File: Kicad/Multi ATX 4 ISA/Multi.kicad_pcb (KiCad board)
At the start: 2 copper layers, 111.8 x 172.7 mm, 88 parts, among them J1 Bus_ISA_8bit, J10 Conn_02x08_Counter_Clockwise, J2 Mini-DIN-6, J3 SPK, J5 IRQ6 EN, J6 PWR ON, J7 Bus_ISA_8bit, J8 Bus_ISA_8bit, J9 Bus_ISA_8bit, SW1 RESET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

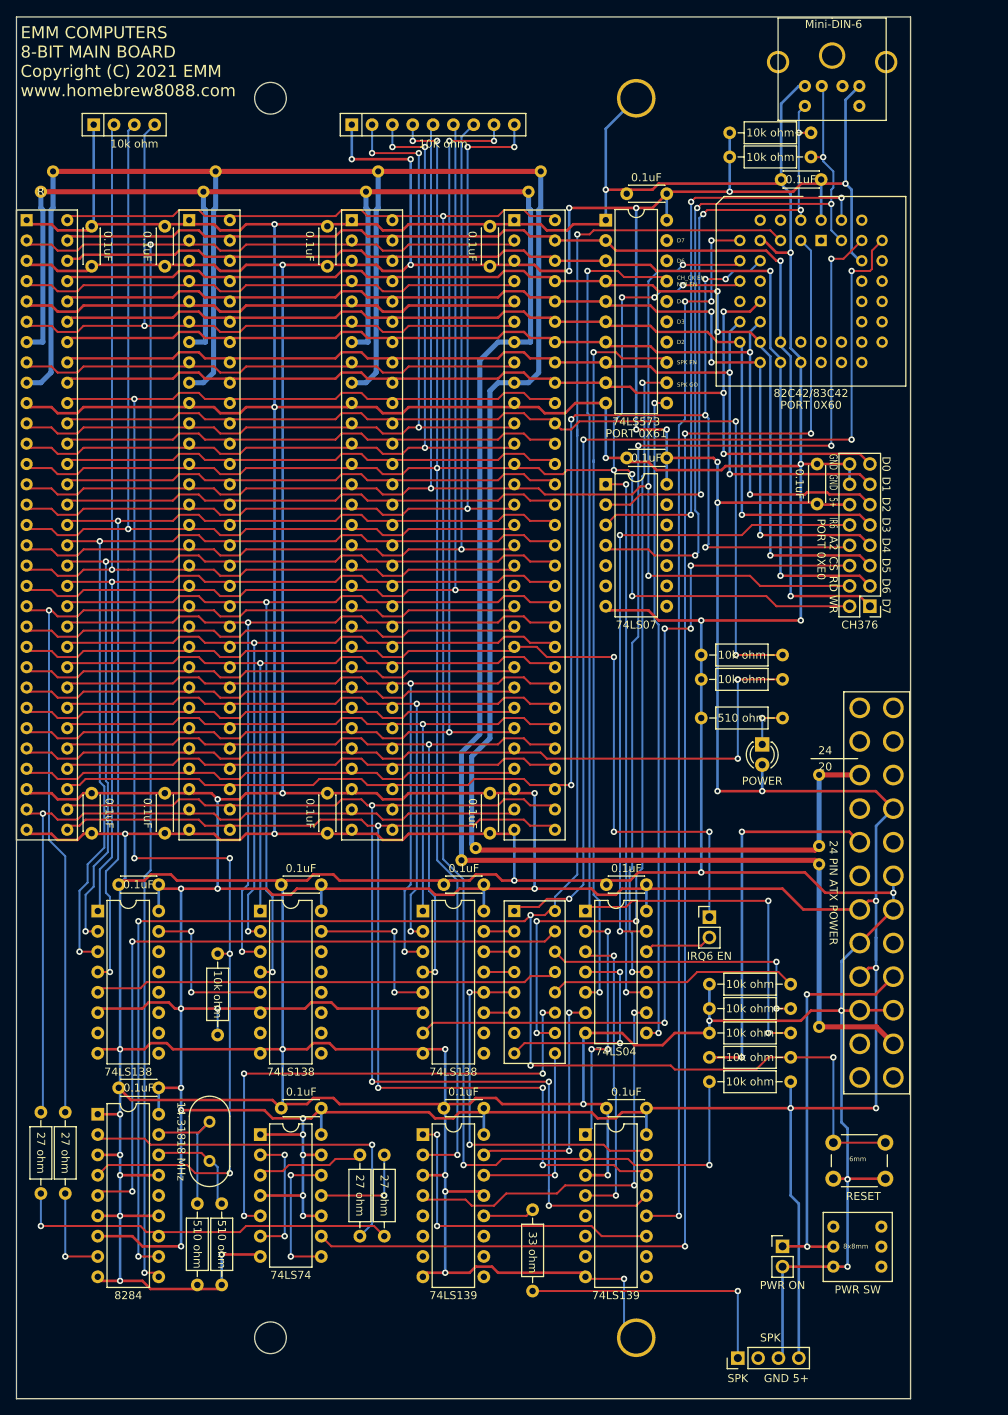
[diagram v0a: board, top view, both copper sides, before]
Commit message: Added port 0x61 read to 4 slot main board
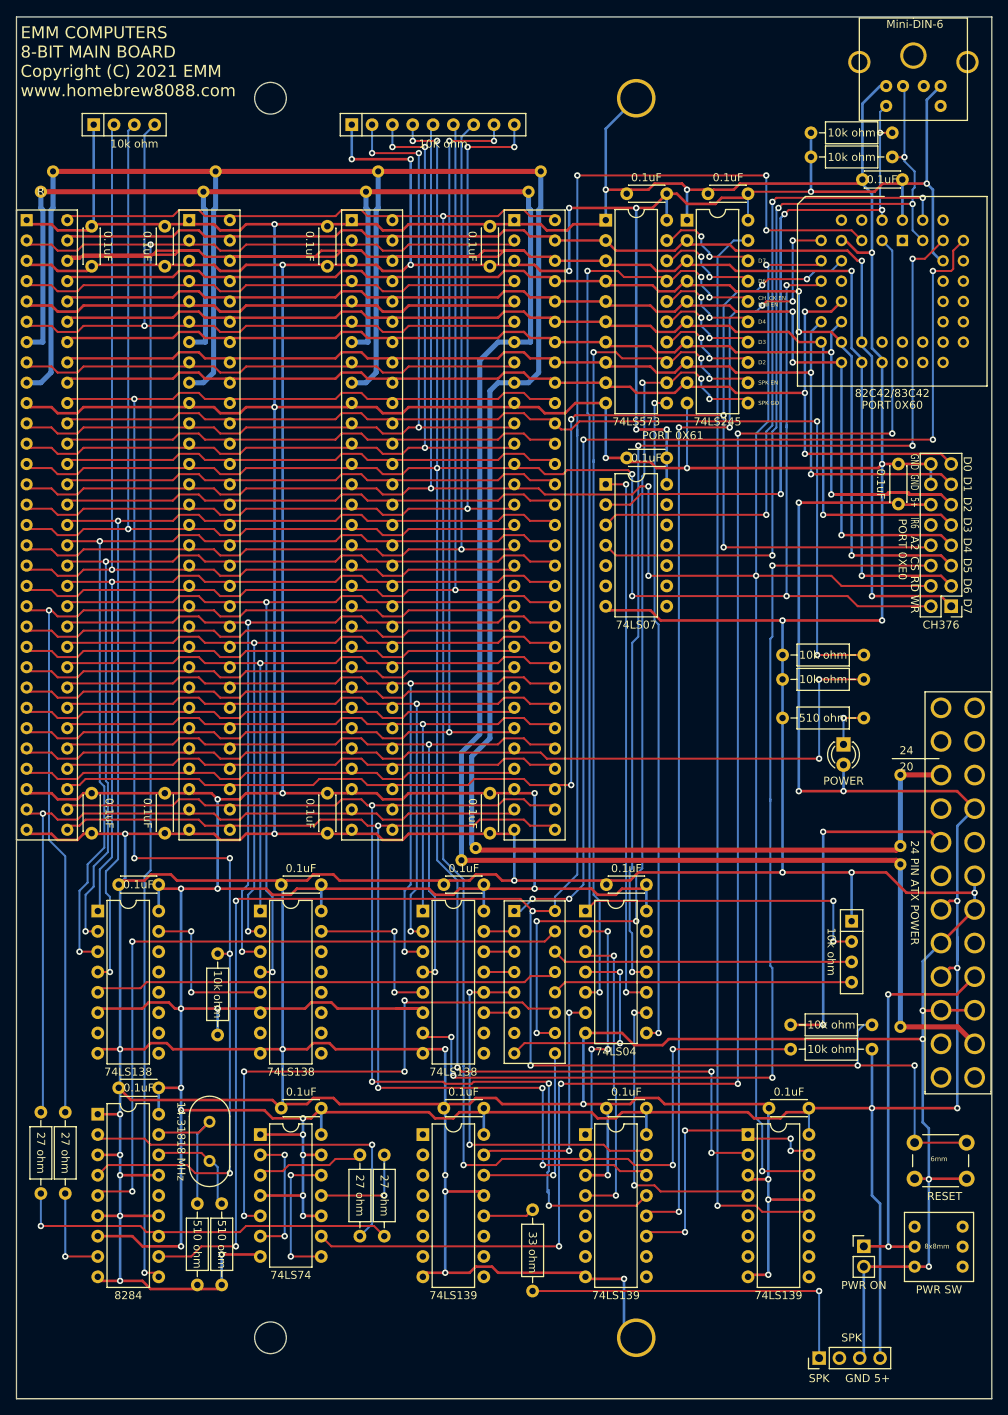
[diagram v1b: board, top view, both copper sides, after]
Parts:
- removed J5: IRQ6 EN, Connector_PinHeader_2.54mm:PinHeader_1x02_P2.54mm_Vertical
- removed R10, R11, R15: 10k ohm, Resistor_THT:R_Axial_DIN0207_L6.3mm_D2.5mm_P10.16mm_Horizontal
- added C11: 0.1uF, Capacitor_THT:C_Disc_D4.3mm_W1.9mm_P5.00mm, F.Cu at (106.5, 40.6)
- added C13: 0.1uF, Capacitor_THT:C_Disc_D4.3mm_W1.9mm_P5.00mm, F.Cu at (114.1, 154.9)
- added RN3: 10k ohm, Resistor_THT:R_Array_SIP4, F.Cu at (124.5, 131.6)
- added U1: 74LS139, Package_DIP:DIP-16_W7.62mm, F.Cu at (111.5, 158.2)
- added U2: 74LS245, Package_DIP:DIP-20_W7.62mm, F.Cu at (103.9, 43.9)
- moved R5 10.9 mm to (116.8, 144.5)
- moved R7 10.9 mm to (127.0, 147.6)
- moved ? 10.2 mm to (145.3, 60.5)
- moved CH376 10.2 mm to (136.9, 92.2)
- moved R 10.2 mm to (130.6, 113.3)
- moved R 10.2 mm to (130.6, 122.2)
- moved R 10.2 mm to (130.6, 144.8)
- moved R 10.2 mm to (130.6, 124.5)
- moved 8x8mm1 10.2 mm to (132.3, 169.8)
- moved ATXPOWER1 10.2 mm to (135.6, 104.9)
- moved C10 10.2 mm to (130.3, 74.4)
- moved C9 10.2 mm to (125.8, 38.9)
- moved D1 10.2 mm to (123.4, 109.5)
- moved J2 10.2 mm to (128.8, 27.2)
- moved J3 10.2 mm to (120.4, 186.2)
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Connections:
- U117 pad 1: /IO_0061 -> Net-(U117-Pad1)
- U117 pad 2: /IOWR -> Net-(U117-Pad2)
- U117 pad 3: /GND -> Net-(U117-Pad3)
- U117 pad 4: /PORT_0X61_EN -> Net-(U117-Pad4)
- U15 pad 14: Net-(U15-Pad14) -> /PORT_61_2
- U15 pad 15: Net-(U15-Pad15) -> /PORT_61_3
- U15 pad 16: Net-(U15-Pad16) -> /PORT_61_4
- U15 pad 18: Net-(U15-Pad18) -> /PORT_61_6
- U15 pad 19: Net-(U15-Pad19) -> /PORT_61_7
- U16 pad 12: /IRQ6_JMP -> Net-(U16-Pad12)
- U16 pad 13: /IN_IRQ6 -> Net-(U16-Pad13)
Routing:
- net /PORT_61_RD: track 0.00 -> 135.2 mm, vias 0 -> 1
- net /GND: track 1082.1 -> 1196.7 mm, vias 32 -> 38
- net /IORD: track 202.4 -> 302.2 mm, vias 4 -> 6
- net /IN_IRQ6: track 82.1 -> 0.00 mm, vias 2 -> 0
- net /D6: track 141.9 -> 202.6 mm
- net /IRQ6: track 121.5 -> 64.1 mm, vias 3 -> 0
- net /IOWR: track 297.5 -> 345.4 mm
- net /T0: track 76.4 -> 121.6 mm
- net /RESET: track 284.3 -> 323.3 mm, vias 6 -> 9
- net /D2: track 126.9 -> 152.7 mm
- net /IO_00EX: track 111.0 -> 133.0 mm
- net /A2: track 188.9 -> 205.3 mm
- net /CH_CK: track 226.0 -> 240.9 mm, vias 3 -> 4
- net /PORT_0X61_EN: track 51.1 -> 37.9 mm
- net /SPK_GO: track 99.6 -> 112.7 mm, vias 4 -> 6
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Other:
- board size 111.8 x 172.7 mm -> 121.9 x 172.7 mm

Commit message: Updated Gerber files
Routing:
- net /5+: track 883.4 -> 939.1 mm, vias 34 -> 35
- net /D6: track 202.6 -> 160.9 mm
- net /A1: track 150.0 -> 147.6 mm
- net /D2: track 152.7 -> 152.0 mm
- net /CH_CK: track 240.9 -> 240.2 mm
- net /AEN: track 133.4 -> 132.7 mm
- net /A2: track 205.3 -> 204.6 mm
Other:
- board text added: "EMM COMPUTERS 8-BIT MAIN BOARD Copyright (C) 2022 EMM www.homebrew8088.com"
- board text removed: "EMM COMPUTERS 8-BIT MAIN BOARD Copyright (C) 2021 EMM www.homebrew8088.com"
